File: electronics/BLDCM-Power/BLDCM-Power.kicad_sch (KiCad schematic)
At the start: 37 parts, among them J1 501920-3001, J2 53048-0310, J3 53261-0471, J4 53261-0471, J5 FTSH-107-01-L-DV-K, J6 12402012E212A, U1 INA239-Q1, U2 LDL212PV33R, U3 TMC6300-LA, U4 INA239-Q1, U5 TCAN1462, U6 INA239-Q1

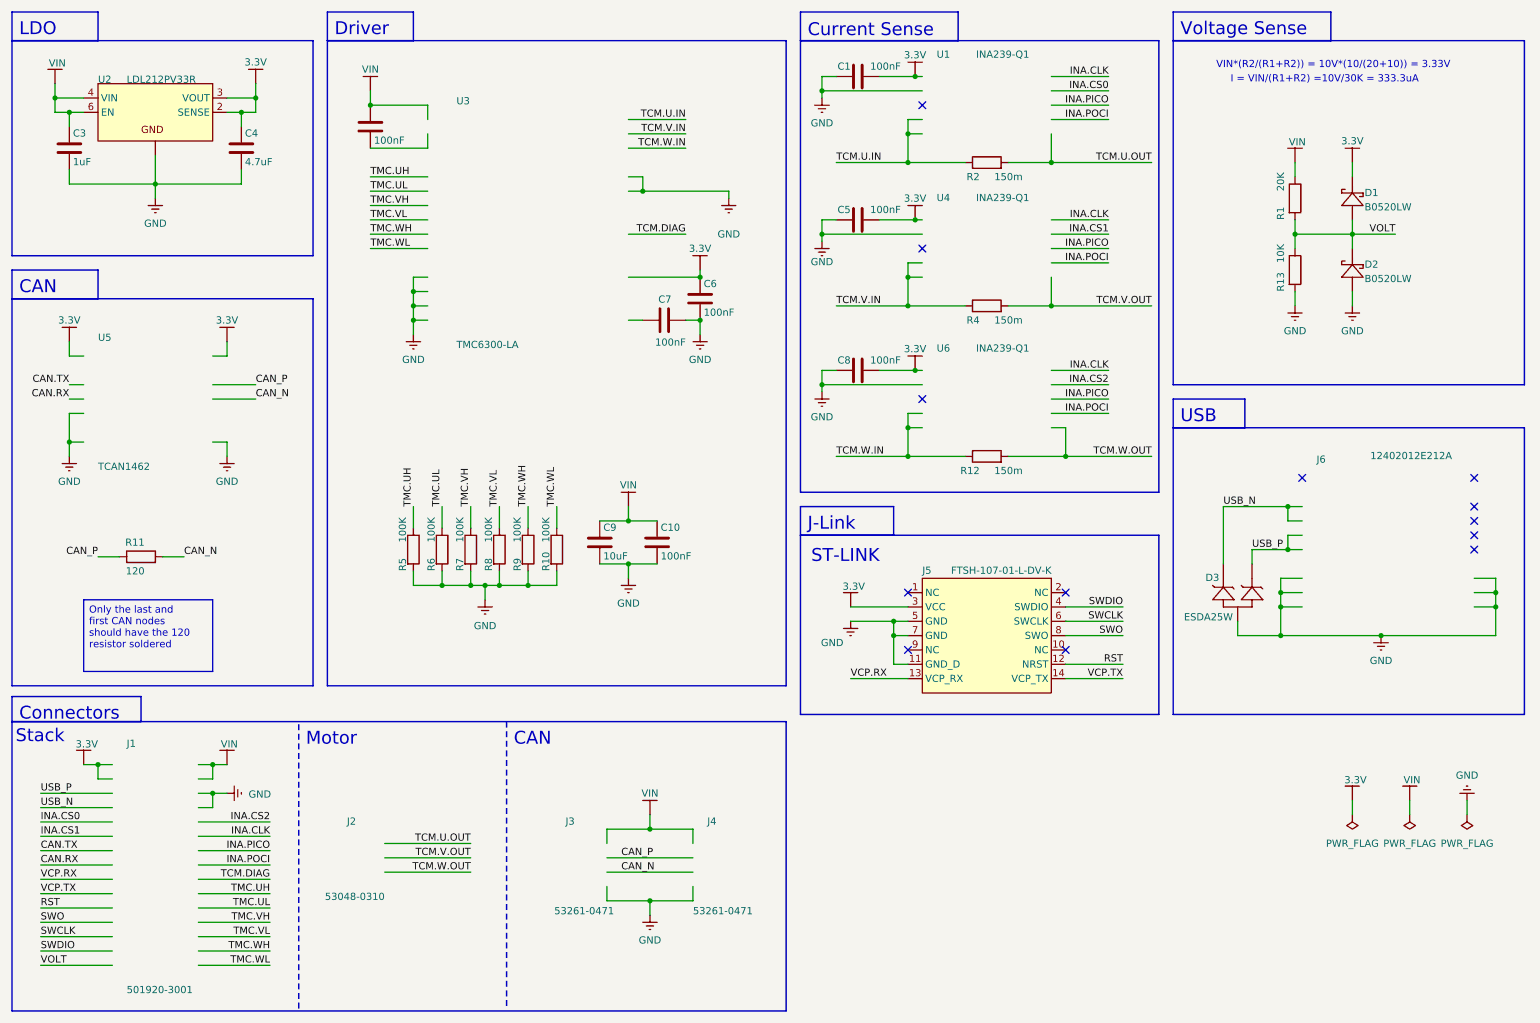
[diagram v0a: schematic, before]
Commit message: Feat: Power PCB replace symbols with brenocq lib symbols
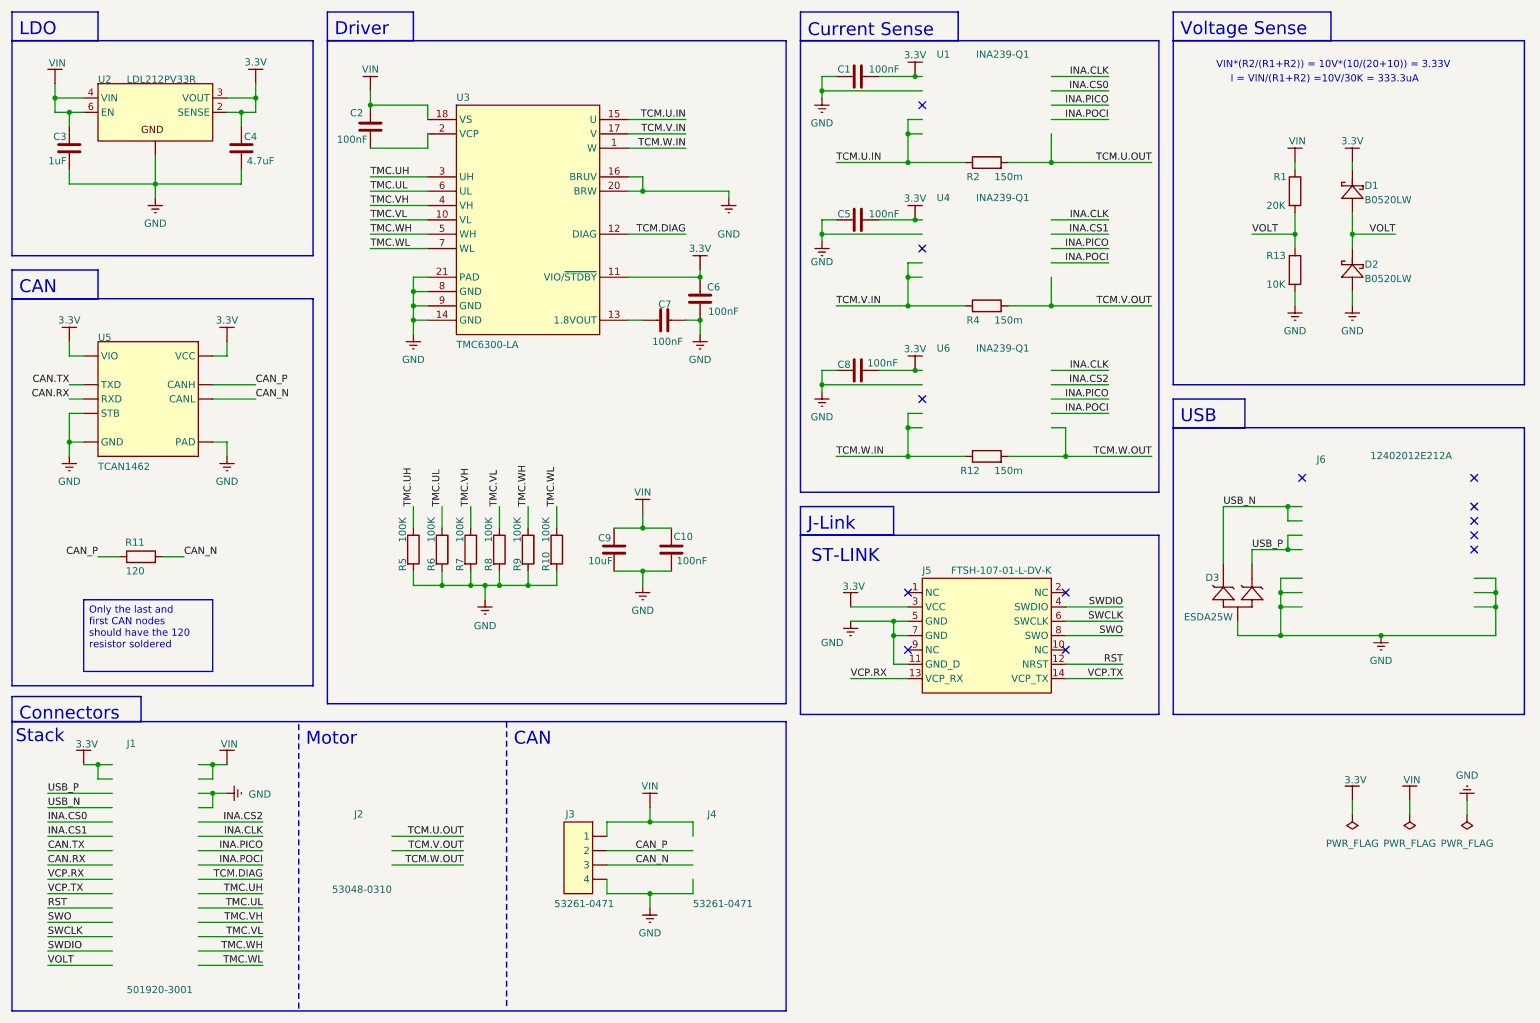
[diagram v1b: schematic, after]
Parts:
- C1, C10, C2, C5, C6, C7, C8: symbol Device:C -> BrenoCQ:C
- C3, C4: footprint BrenoCQ:C_0603 -> BrenoCQ:C_0402; symbol Device:C -> BrenoCQ:C
- C9: footprint BrenoCQ:C_0805 -> BrenoCQ:C_0402; symbol Device:C -> BrenoCQ:C
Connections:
- net 3.3V: now also C1.1, C4.2, C5.1, C6.2, C8.1, U3.11 (VIO/~{STDBY}), U5.3 (VCC), U5.5 (VIO); no longer C1.2, C4.1, C5.2, C6.1, C8.2
- net CAN.RX: now also U5.4 (RXD)
- net CAN.TX: now also U5.1 (TXD)
- net CAN_N: now also J3.3, U5.6 (CANL)
- net CAN_P: now also J3.2, U5.7 (CANH)
- net GND: now also C1.2, C10.1, C3.1, C4.1, C5.2, C6.1, C7.1, C8.2, C9.1, J3.4, U3.14 (GND), U3.16 (BRUV), U3.20 (BRW), U3.21 (PAD), U3.8 (GND), U3.9 (GND), U5.2 (GND), U5.8 (STB), U5.PAD; no longer C1.1, C10.2, C3.2, C4.2, C5.1, C6.2, C7.2, C8.1, C9.2
- net TCM.DIAG: now also U3.12 (DIAG)
- net TCM.U.IN: now also U3.15 (U)
- net TCM.V.IN: now also U3.17 (V)
- net TCM.W.IN: now also U3.1 (W)
- net TMC.UH: now also U3.3 (UH)
- net TMC.UL: now also U3.6 (UL)
- net TMC.VH: now also U3.4 (VH)
- net TMC.VL: now also U3.10 (VL)
- net TMC.WH: now also U3.5 (WH)
- net TMC.WL: now also U3.7 (WL)
- net VIN: now also C10.2, C2.2, C3.2, C9.2, J3.1, U3.18 (VS); no longer C10.1, C2.1, C3.1, C9.1
- new net: C2.1, U3.2 (VCP)
- new net: C7.2, U3.13 (1.8VOUT)
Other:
- moved on the sheet: D1, R1

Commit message: Feat(pcb): Create net classes in power PCB
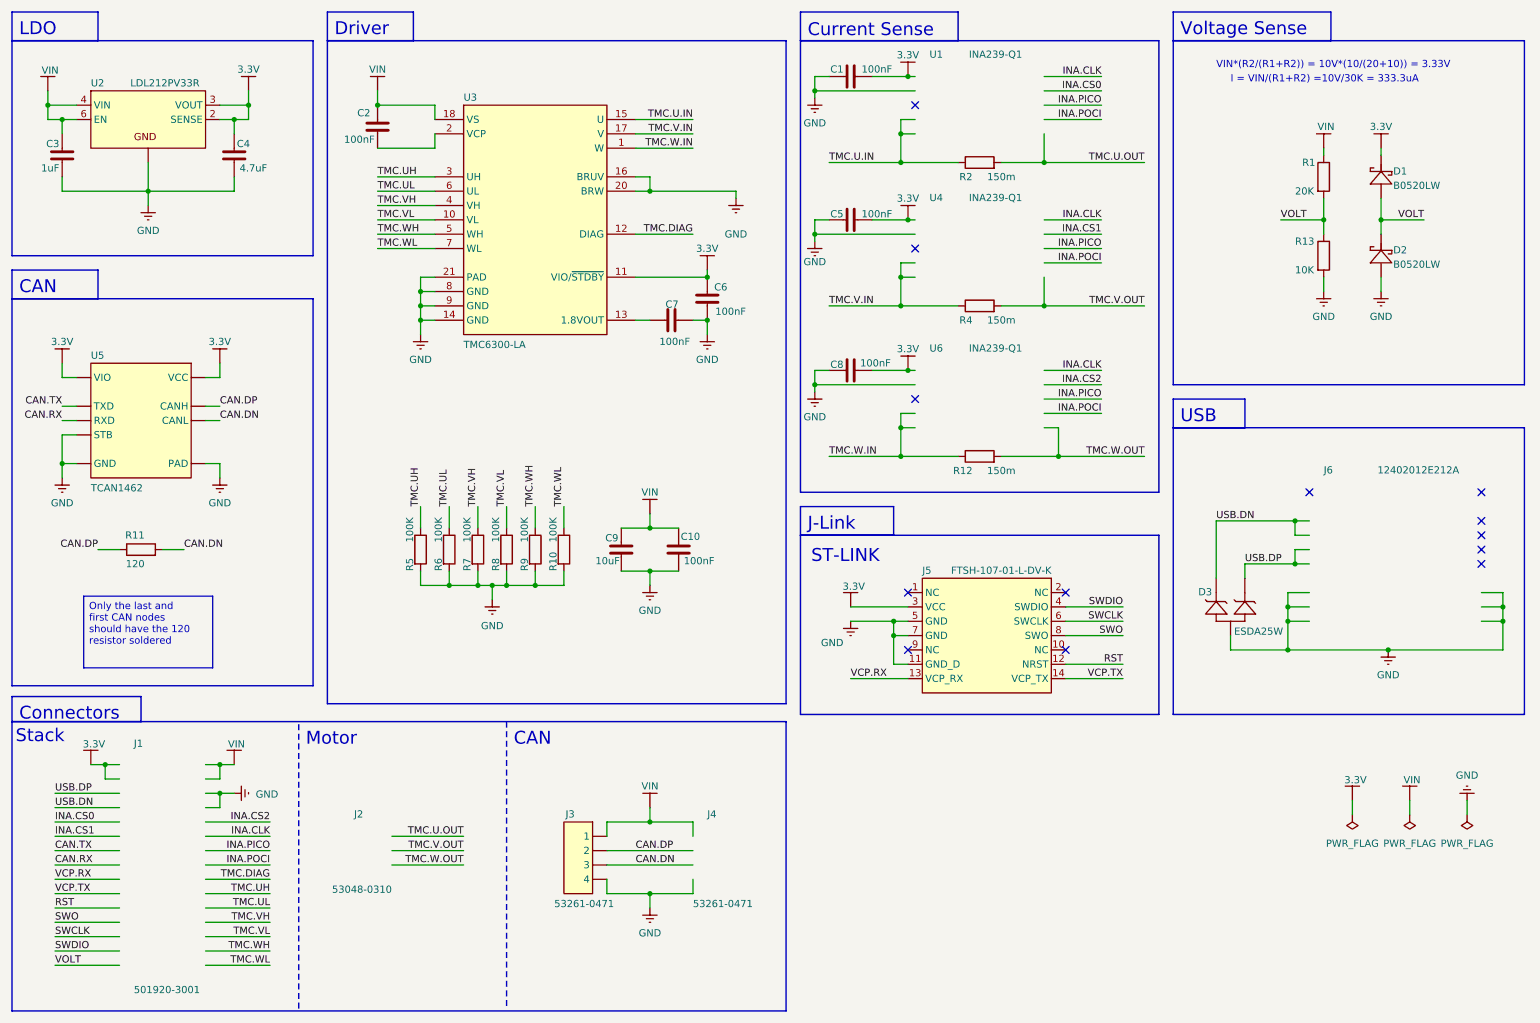
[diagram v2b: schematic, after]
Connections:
- net CAN_N renamed CAN.DN
- net CAN_P renamed CAN.DP
- net TCM.DIAG renamed TMC.DIAG
- net TCM.U.IN renamed TMC.U.IN
- net TCM.U.OUT renamed TMC.U.OUT
- net TCM.V.IN renamed TMC.V.IN
- net TCM.V.OUT renamed TMC.V.OUT
- net TCM.W.IN renamed TMC.W.IN
- net TCM.W.OUT renamed TMC.W.OUT
- net USB_N renamed USB.DN
- net USB_P renamed USB.DP
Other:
- moved on the sheet: C1, C10, C2, C3, C4, C5, C6, C7, C8, C9, D1, D2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

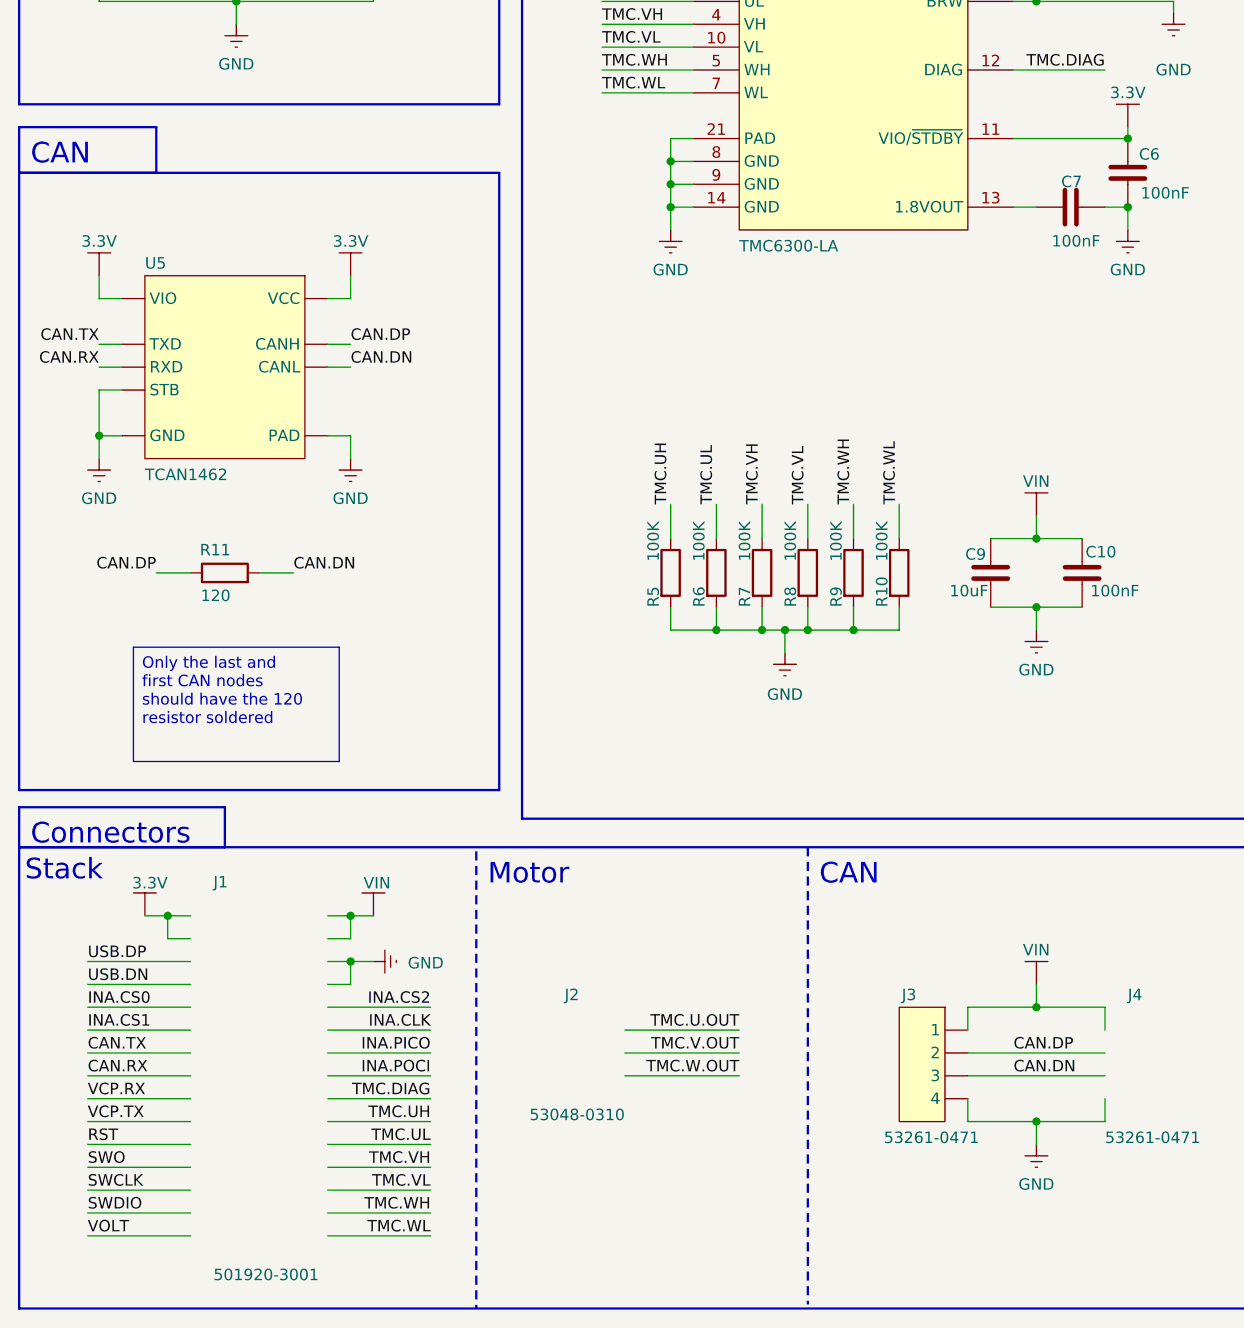
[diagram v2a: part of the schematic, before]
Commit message: Feat(pcb): Route differential pairs in Power PCB
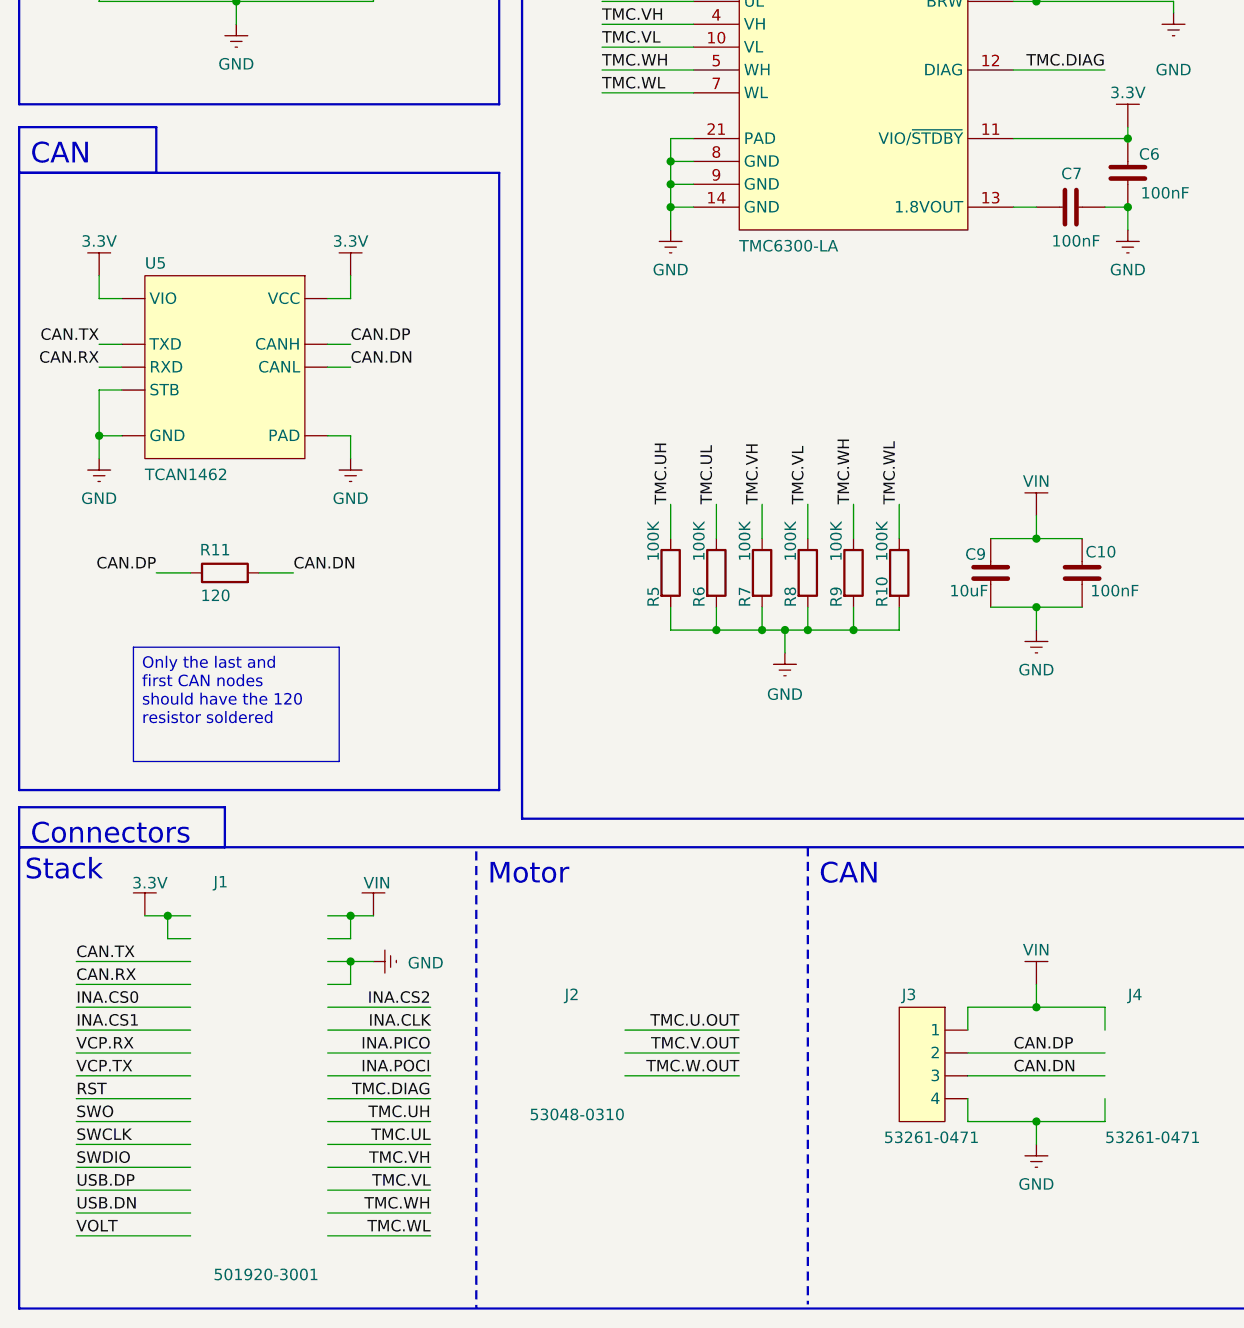
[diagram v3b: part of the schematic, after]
